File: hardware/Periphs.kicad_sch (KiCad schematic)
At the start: 0 parts

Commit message: poop
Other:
- note added: "CAN -> SPI TCAN4550-Q1 Add ESD/TVS for accidental 24V on CAN line + n shit"
- note removed: "CAN -> SPI n shit"
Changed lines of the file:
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@@
 	(generator_version "10.0")
 	(paper "A4")
-	(text "CAN -> SPI\nn shit"
+	(text "CAN -> SPI\n	TCAN4550-Q1\n	Add ESD/TVS for accidental 24V on CAN line\n\n\n+ n shit\n	"
 		(exclude_from_sim no)
-		(at 129.032 96.52 0)
+		(at 86.868 85.09 0)
 		(effects
 			(font

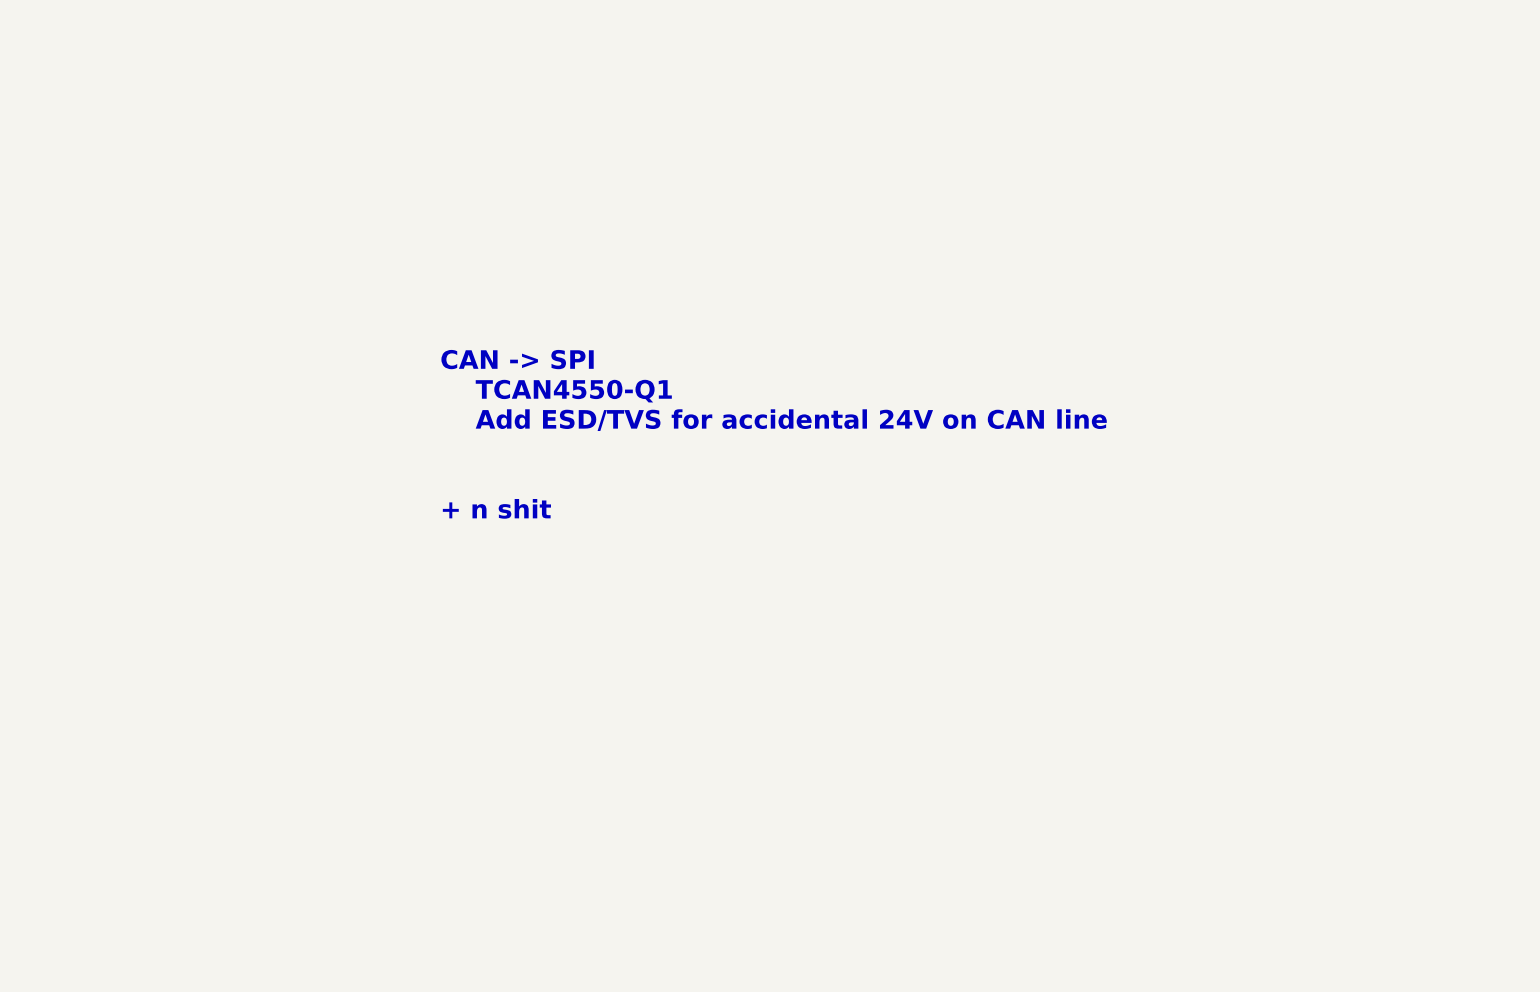
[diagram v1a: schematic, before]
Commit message: added can spi
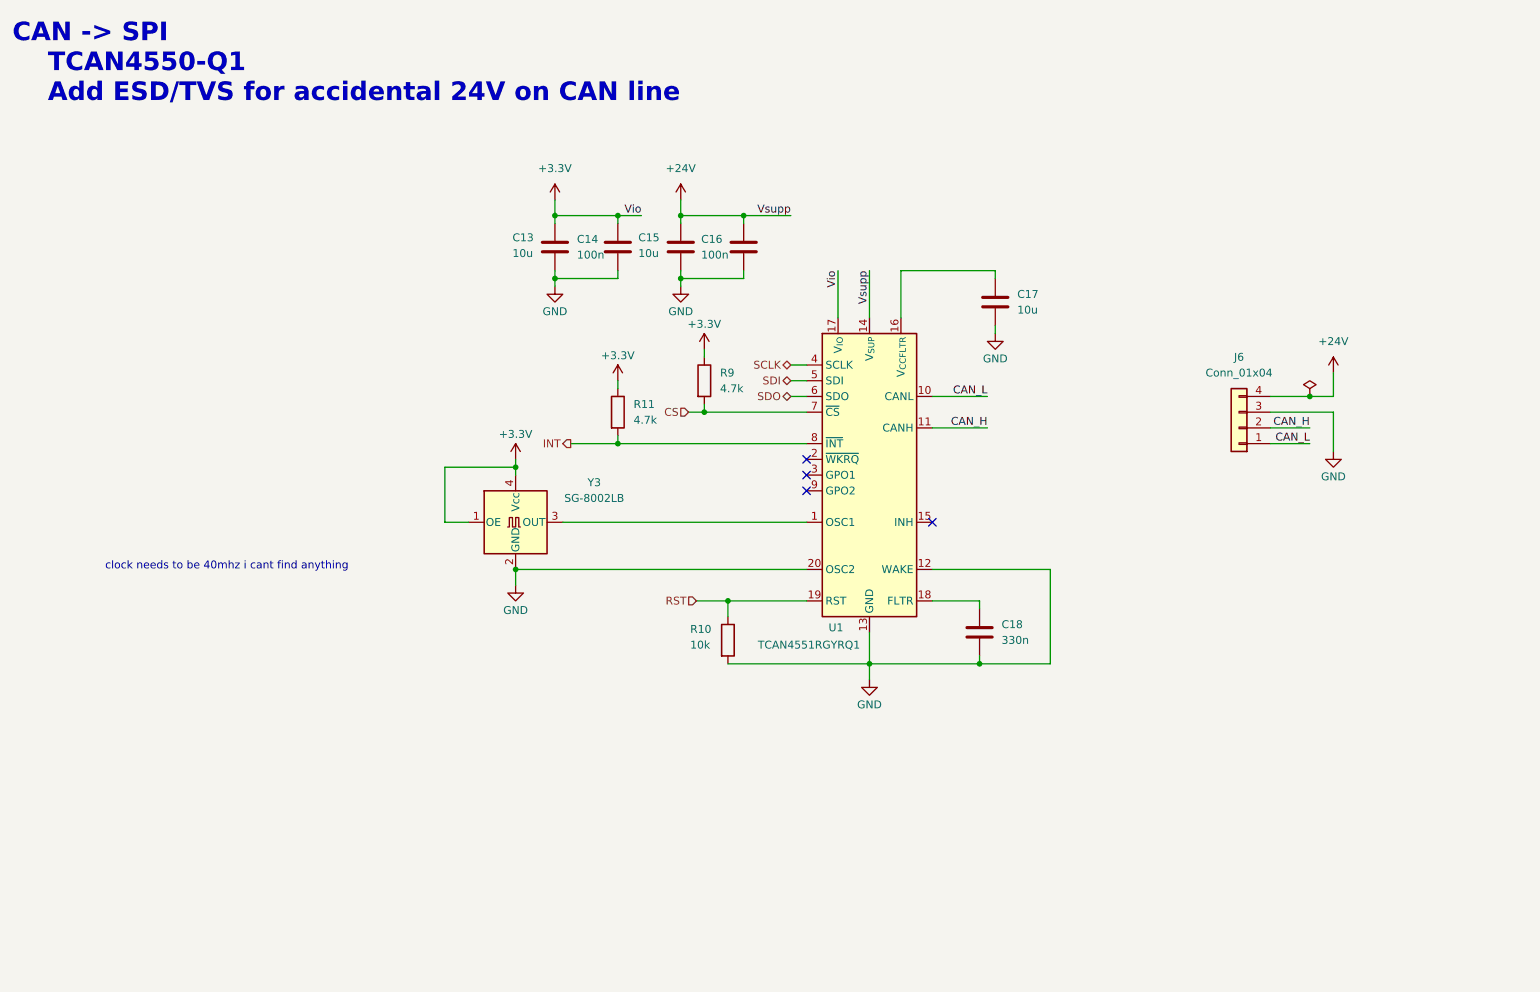
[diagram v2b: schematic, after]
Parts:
- added C13, C15, C17: 10u, symbol Device:C
- added C14, C16: 100n, symbol Device:C
- added C18: 330n, symbol Device:C
- added J6: Conn_01x04, symbol Connector_Generic:Conn_01x04
- added R10: 10k, symbol Device:R
- added R11, R9: 4.7k, symbol Device:R
- added U1: TCAN4551RGYRQ1, Package_DFN_QFN:Texas_RGY_R-PVQFN-N20_EP2.05x3.05mm, symbol Interface_CAN_LIN:TCAN4551RGYRQ1
- added Y3: SG-8002LB, Oscillator:Oscillator_SMD_SeikoEpson_SG8002LB-4Pin_5.0x3.2mm, symbol Oscillator:SG-8002LB
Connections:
- new net: U1.1 (OSC1), Y3.3 (OUT)
- new net: C18.1, U1.18 (FLTR)
- new net: C17.1, U1.16 (V_{CCFLTR})
- new net +24V: C15.1, C16.1, J6.4 (Pin_4), U1.14 (V_{SUP})
- new net +3.3V: C13.1, C14.1, R11.1, R9.1, U1.17 (V_{IO}), Y3.1 (OE), Y3.4 (Vcc)
- new net CAN_H: J6.2 (Pin_2), U1.11 (CANH)
- new net CAN_L: J6.1 (Pin_1), U1.10 (CANL)
- new net CS: R9.2, U1.7 (~{CS})
- new net GND: C13.2, C14.2, C15.2, C16.2, C17.2, C18.2, J6.3 (Pin_3), R10.2, U1.12 (WAKE), U1.13 (GND), U1.20 (OSC2), U1.21 (GND), Y3.2 (GND)
- new net INT: R11.2, U1.8 (~{INT})
- new net RST: R10.1, U1.19 (RST)
- new net SCLK: U1.4 (SCLK)
- new net SDI: U1.5 (SDI)
- new net SDO: U1.6 (SDO)
- no-connect marks 0 -> 4
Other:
- note added: "CAN -> SPI TCAN4550-Q1 Add ESD/TVS for accidental 24V on CAN line"
- note added: "clock needs to be 40mhz i cant find anything"
- note removed: "CAN -> SPI TCAN4550-Q1 Add ESD/TVS for accidental 24V on CAN line + n shit"

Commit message: some changes`
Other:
- moved on the sheet: C18, Y3
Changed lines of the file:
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@@
 	)
 	(junction
-		(at 99.06 104.14)
+		(at 115.57 83.82)
 		(diameter 0)
 		(color 0 0 0 0)
 	)
 	(junction
-		(at 115.57 83.82)
+		(at 96.52 105.41)
 		(diameter 0)
 		(color 0 0 0 0)
@@
 	)
 	(junction
-		(at 173.99 119.38)
+		(at 96.52 87.63)
 		(diameter 0)
 		(color 0 0 0 0)
 	)
 	(junction
-		(at 99.06 87.63)
+		(at 105.41 46.99)
 		(diameter 0)
 		(color 0 0 0 0)
 	)
 	(junction
-		(at 105.41 46.99)
+		(at 175.26 119.38)
 		(diameter 0)
 		(color 0 0 0 0)
@@
 	(wire
 		(pts
-			(xy 173.99 109.22) (xy 173.99 110.49)
+			(xy 175.26 109.22) (xy 175.26 110.49)
 		)
 		(stroke
@@
 	(wire
 		(pts
-			(xy 99.06 86.36) (xy 99.06 87.63)
+			(xy 96.52 86.36) (xy 96.52 87.63)
 		)
 		(stroke
@@
 	(wire
 		(pts
-			(xy 166.37 109.22) (xy 173.99 109.22)
+			(xy 139.7 105.41) (xy 139.7 104.14)
 		)
 		(stroke
@@
 	(wire
 		(pts
-			(xy 125.73 57.15) (xy 135.89 57.15)
+			(xy 166.37 109.22) (xy 175.26 109.22)
 		)
 		(stroke
@@
 	(wire
 		(pts
-			(xy 105.41 44.45) (xy 105.41 46.99)
+			(xy 125.73 57.15) (xy 135.89 57.15)
 		)
 		(stroke
@@
 	(wire
 		(pts
-			(xy 156.21 119.38) (xy 173.99 119.38)
+			(xy 105.41 44.45) (xy 105.41 46.99)
 		)
 		(stroke
@@
 	(wire
 		(pts
-			(xy 105.41 46.99) (xy 115.57 46.99)
+			(xy 156.21 119.38) (xy 175.26 119.38)
 		)
 		(stroke
@@
 	(wire
 		(pts
-			(xy 220.98 83.82) (xy 227.33 83.82)
+			(xy 105.41 46.99) (xy 115.57 46.99)
 		)
 		(stroke
@@
 	(wire
 		(pts
-			(xy 173.99 118.11) (xy 173.99 119.38)
+			(xy 220.98 83.82) (xy 227.33 83.82)
 		)
 		(stroke
@@
 	(wire
 		(pts
-			(xy 185.42 119.38) (xy 173.99 119.38)
+			(xy 125.73 48.26) (xy 125.73 46.99)
 		)
 		(stroke
@@
 	(wire
 		(pts
-			(xy 99.06 104.14) (xy 146.05 104.14)
+			(xy 105.41 57.15) (xy 105.41 58.42)
 		)
 		(stroke
@@
 	(wire
 		(pts
-			(xy 125.73 48.26) (xy 125.73 46.99)
+			(xy 125.73 57.15) (xy 125.73 58.42)
 		)
 		(stroke
@@
 	(wire
 		(pts
-			(xy 105.41 57.15) (xy 105.41 58.42)
+			(xy 156.21 119.38) (xy 156.21 121.92)
 		)
 		(stroke
@@
 	(wire
 		(pts
-			(xy 125.73 57.15) (xy 125.73 58.42)
+			(xy 96.52 105.41) (xy 139.7 105.41)
 		)
 		(stroke
@@
 	(wire
 		(pts
-			(xy 156.21 119.38) (xy 156.21 121.92)
+			(xy 143.51 73.66) (xy 146.05 73.66)
 		)
 		(stroke
@@
 	(wire
 		(pts
-			(xy 143.51 73.66) (xy 146.05 73.66)
+			(xy 129.54 77.47) (xy 129.54 78.74)
 		)
 		(stroke
@@
 	(wire
 		(pts
-			(xy 129.54 77.47) (xy 129.54 78.74)
+			(xy 127 78.74) (xy 129.54 78.74)
 		)
 		(stroke
@@
 	(wire
 		(pts
-			(xy 127 78.74) (xy 129.54 78.74)
+			(xy 125.73 44.45) (xy 125.73 46.99)
 		)
 		(stroke
@@
 	(wire
 		(pts
-			(xy 125.73 44.45) (xy 125.73 46.99)
+			(xy 125.73 46.99) (xy 135.89 46.99)
 		)
 		(stroke
@@
 	(wire
 		(pts
-			(xy 125.73 46.99) (xy 135.89 46.99)
+			(xy 85.09 87.63) (xy 96.52 87.63)
 		)
 		(stroke
@@
 	(wire
 		(pts
-			(xy 87.63 87.63) (xy 99.06 87.63)
+			(xy 156.21 55.88) (xy 156.21 63.5)
 		)
 		(stroke
@@
 	(wire
 		(pts
-			(xy 156.21 55.88) (xy 156.21 63.5)
+			(xy 175.26 118.11) (xy 175.26 119.38)
 		)
 		(stroke
@@
 	(wire
 		(pts
-			(xy 91.44 96.52) (xy 87.63 96.52)
+			(xy 88.9 96.52) (xy 85.09 96.52)
 		)
 		(stroke
@@
 	(wire
 		(pts
-			(xy 87.63 96.52) (xy 87.63 87.63)
+			(xy 85.09 96.52) (xy 85.09 87.63)
 		)
 		(stroke
@@
 	(wire
 		(pts
-			(xy 133.35 109.22) (xy 146.05 109.22)
+			(xy 139.7 104.14) (xy 146.05 104.14)
 		)
 		(stroke
@@
 	(wire
 		(pts
-			(xy 99.06 104.14) (xy 99.06 106.68)
+			(xy 96.52 105.41) (xy 96.52 104.14)
+		)
+		(stroke
+			(width 0)
+			(type default)
+		)
+	)
+	(wire
+		(pts
+			(xy 133.35 109.22) (xy 146.05 109.22)
 		)
 		(stroke
@@
 	(wire
 		(pts
-			(xy 106.68 96.52) (xy 146.05 96.52)
+			(xy 104.14 96.52) (xy 146.05 96.52)
 		)
 		(stroke
@@
 	(wire
 		(pts
+			(xy 175.26 119.38) (xy 185.42 119.38)
+		)
+		(stroke
+			(width 0)
+			(type default)
+		)
+	)
+	(wire
+		(pts
 			(xy 220.98 76.2) (xy 227.33 76.2)
 		)
@@
 	(wire
 		(pts
-			(xy 99.06 87.63) (xy 99.06 88.9)
+			(xy 96.52 105.41) (xy 96.52 107.95)
+		)
+		(stroke
+			(width 0)
+			(type default)
+		)
+	)
+	(wire
+		(pts
+			(xy 96.52 87.63) (xy 96.52 88.9)
 		)
 		(stroke
@@
 	)
 	(image
-		(at 157.48 129.54)
+		(at 157.48 132.08)
 		(scale 0.238773)
 		(data "iVBORw0KGgoAAAANSUhEUgAABqIAAACCCAYAAAAt69luAAAMTWlDQ1BJQ0MgUHJvZmlsZQAASImV"
@@
 		)
 		(property "Value" "GND"
-			(at 156.21 125.984 0)
+			(at 156.21 125.476 0)
 			(show_name no)
 			(do_not_autoplace no)
@@
 	(symbol
 		(lib_id "power:+3.3V")
-		(at 99.06 86.36 0)
+		(at 96.52 86.36 0)
 		(unit 1)
 		(body_style 1)
@@
 		(dnp no)
 		(property "Reference" "#PWR039"
-			(at 99.06 90.17 0)
+			(at 96.52 90.17 0)
 			(hide yes)
 			(show_name no)
@@
 		)
 		(property "Value" "+3.3V"
-			(at 99.06 82.296 0)
+			(at 96.52 82.804 0)
 			(show_name no)
 			(do_not_autoplace no)
@@
 		)
 		(property "Footprint" ""
-			(at 99.06 86.36 0)
+			(at 96.52 86.36 0)
 			(hide yes)
 			(show_name no)
@@
 		)
 		(property "Datasheet" ""
-			(at 99.06 86.36 0)
+			(at 96.52 86.36 0)
 			(hide yes)
 			(show_name no)
@@
 		)
 		(property "Description" "Power symbol creates a global label with name \"+3.3V\""
-			(at 99.06 86.36 0)
+			(at 96.52 86.36 0)
 			(hide yes)
 			(show_name no)
@@
 	(symbol
 		(lib_id "Oscillator:SG-8002LB")
-		(at 99.06 96.52 0)
+		(at 96.52 96.52 0)
 		(unit 1)
 		(body_style 1)
@@
 		(in_pos_files yes)
 		(dnp no)
-		(fields_autoplaced yes)
 		(property "Reference" "Y3"
-			(at 111.76 90.0998 0)
+			(at 107.696 97.79 0)
 			(show_name no)
 			(do_not_autoplace no)
@@
 		)
 		(property "Value" "SG-8002LB"
-			(at 111.76 92.6398 0)
+			(at 107.696 100.33 0)
 			(show_name no)
 			(do_not_autoplace no)
@@
 		)
 		(property "Footprint" "Oscillator:Oscillator_SMD_SeikoEpson_SG8002LB-4Pin_5.0x3.2mm"
-			(at 116.84 105.41 0)
+			(at 114.3 105.41 0)
 			(hide yes)
 			(show_name no)
@@
 		)
 		(property "Datasheet" "https://support.epson.biz/td/api/doc_check.php?dl=brief_SG-8002LB&lang=en"
-			(at 96.52 96.52 0)
+			(at 93.98 96.52 0)
 			(hide yes)
 			(show_name no)
@@
 		)
 		(property "Description" "CMOS Clock Oscillator 1 to 125 MHz"
-			(at 99.06 96.52 0)
+			(at 96.52 96.52 0)
 			(hide yes)
 			(show_name no)
@@
 	(symbol
 		(lib_id "Device:C")
-		(at 173.99 114.3 0)
+		(at 175.26 114.3 0)
 		(unit 1)
 		(body_style 1)
@@
 		(dnp no)
 		(property "Reference" "C18"
-			(at 177.546 113.03 0)
+			(at 177.8 113.03 0)
 			(show_name no)
 			(do_not_autoplace no)
@@
 		)
 		(property "Value" "330n"
-			(at 177.546 115.57 0)
+			(at 177.8 115.57 0)
 			(show_name no)
 			(do_not_autoplace no)
@@
 		)
 		(property "Footprint" ""
-			(at 174.9552 118.11 0)
+			(at 176.2252 118.11 0)
 			(hide yes)
 			(show_name no)
@@
 		)
 		(property "Datasheet" ""
-			(at 173.99 114.3 0)
+			(at 175.26 114.3 0)
 			(hide yes)
 			(show_name no)
@@
 		)
 		(property "Description" "Unpolarized capacitor"
-			(at 173.99 114.3 0)
+			(at 175.26 114.3 0)
 			(hide yes)
 			(show_name no)
@@
 	(symbol
 		(lib_id "power:GND")
-		(at 99.06 106.68 0)
+		(at 96.52 107.95 0)
 		(unit 1)
 		(body_style 1)
@@
 		(dnp no)
 		(property "Reference" "#PWR040"
-			(at 99.06 113.03 0)
+			(at 96.52 114.3 0)
 			(hide yes)
 			(show_name no)
@@
 		)
 		(property "Value" "GND"
-			(at 99.06 110.744 0)
+			(at 96.52 112.014 0)
 			(show_name no)
 			(do_not_autoplace no)
@@
 		)
 		(property "Footprint" ""
-			(at 99.06 106.68 0)
+			(at 96.52 107.95 0)
 			(hide yes)
 			(show_name no)
@@
 		)
 		(property "Datasheet" ""
-			(at 99.06 106.68 0)
+			(at 96.52 107.95 0)
 			(hide yes)
 			(show_name no)
@@
 		)
 		(property "Description" "Power symbol creates a global label with name \"GND\" , ground"
-			(at 99.06 106.68 0)
+			(at 96.52 107.95 0)
 			(hide yes)
 			(show_name no)

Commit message: clock added
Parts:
- removed Y3: SG-8002LB, Oscillator:Oscillator_SMD_SeikoEpson_SG8002LB-4Pin_5.0x3.2mm, symbol Oscillator:SG-8002LB
- added C20, C21: 18p, symbol Device:C
- added Y2: 7M40000005, 7M27120MAAJT, symbol 7M40000005:7M40000005
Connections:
- net +24V: no longer J6.4 (Pin_4)
- net GND: now also C20.2, C21.2, Y2.2 (GND_1), Y2.4 (GND_2); no longer U1.20 (OSC2)
- net at U1.1 (OSC1): now also C20.1, Y2.3 (CRYSTAL)
- new net: C21.1, U1.20 (OSC2), Y2.1 (CRYSTLA)
- new net +12V: J6.4 (Pin_4)
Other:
- note added: "add power protection block"

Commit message: fix
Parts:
- added JP1: Jumper_2_Small_Open, symbol Jumper:Jumper_2_Small_Open
- added R3: 120, symbol Device:R
- C20, C21: value 18p -> 12p
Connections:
- net CAN_H: now also JP1.1 (A)
- net CAN_L: now also R3.2
- net +24V renamed +12v
- new net: JP1.2 (B), R3.1
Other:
- moved on the sheet: C20

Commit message: mika review usb
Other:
- added sheet USBPD (PD.kicad_sch)
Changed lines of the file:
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@@
 		(in_pos_files yes)
 		(dnp no)
-		(fields_autoplaced yes)
 		(property "Reference" "#PWR033"
 			(at 105.41 48.26 0)
@@
 		)
 		(property "Value" "+3.3V"
-			(at 105.41 39.37 0)
+			(at 105.41 40.132 0)
 			(show_name no)
 			(do_not_autoplace no)
@@
 		(in_pos_files yes)
 		(dnp no)
-		(fields_autoplaced yes)
 		(property "Reference" "#PWR034"
 			(at 125.73 48.26 0)
@@
 		)
 		(property "Value" "+12v"
-			(at 128.27 43.1799 0)
+			(at 123.698 40.894 0)
 			(show_name no)
 			(do_not_autoplace no)
@@
 				)
 			)
+		)
+	)
+	(sheet
+		(at 38.1 137.16)
+		(size 60.96 30.48)
+		(exclude_from_sim no)
+		(in_bom yes)
+		(on_board yes)
+		(dnp no)
+		(fields_autoplaced yes)
+		(stroke
+			(width 0.1524)
+			(type solid)
+		)
+		(fill
+			(color 0 0 0 0)
+		)
+		(property "Sheetname" "USBPD"
+			(at 38.1 136.4484 0)
+			(show_name no)
+			(do_not_autoplace no)
+			(effects
+				(font
+					(size 1.27 1.27)
+				)
+				(justify left bottom)
+			)
+		)
+		(property "Sheetfile" "PD.kicad_sch"
+			(at 38.1 168.2246 0)
+			(show_name no)
+			(do_not_autoplace no)
+			(effects
+				(font
+					(size 1.27 1.27)
+				)
+				(justify left top)
+			)
+		)
+		(instances
+			(project "OTTER"
+				(path "/db2a353b-4a3a-4ce7-8df7-bc33bc3b7cc7/eb093129-c761-474d-99d3-e85b871e9c74"
+					(page "10")
+				)
+			)

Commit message: matthew review or get touched
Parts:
- removed R11: 4.7k, symbol Device:R
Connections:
- net +12v renamed +20v
- net INT: no longer names the net of U1.8 (~{INT})
- no-connect marks 4 -> 5
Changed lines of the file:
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@@
 	)
 	(junction
-		(at 115.57 83.82)
-		(diameter 0)
-		(color 0 0 0 0)
-	)
-	(junction
 		(at 255.27 76.2)
 		(diameter 0)
@@
 	)
 	(no_connect
+		(at 146.05 83.82)
+	)
+	(no_connect
 		(at 146.05 91.44)
 	)
@@
 	(wire
 		(pts
-			(xy 115.57 73.66) (xy 115.57 74.93)
-		)
-		(stroke
-			(width 0)
-			(type default)
-		)
-	)
-	(wire
-		(pts
-			(xy 115.57 83.82) (xy 146.05 83.82)
-		)
-		(stroke
-			(width 0)
-			(type default)
-		)
-	)
-	(wire
-		(pts
 			(xy 161.29 55.88) (xy 176.53 55.88)
 		)
@@
 	(wire
 		(pts
-			(xy 107.95 83.82) (xy 115.57 83.82)
-		)
-		(stroke
-			(width 0)
-			(type default)
-		)
-	)
-	(wire
-		(pts
 			(xy 220.98 78.74) (xy 231.14 78.74)
 		)
@@
 	(wire
 		(pts
-			(xy 115.57 82.55) (xy 115.57 83.82)
-		)
-		(stroke
-			(width 0)
-			(type default)
-		)
-	)
-	(wire
-		(pts
 			(xy 176.53 55.88) (xy 176.53 57.15)
 		)
@@
 		)
 	)
-	(hierarchical_label "INT"
-		(shape output)
-		(at 107.95 83.82 180)
-		(effects
-			(font
-				(size 1.27 1.27)
-			)
-			(justify right)
-		)
-	)
 	(hierarchical_label "SCLK"
 		(shape bidirectional)
@@
 	)
 	(symbol
-		(lib_id "Device:R")
-		(at 115.57 78.74 0)
-		(unit 1)
-		(body_style 1)
-		(exclude_from_sim no)
-		(in_bom yes)
-		(on_board yes)
-		(in_pos_files yes)
-		(dnp no)
-		(fields_autoplaced yes)
-		(property "Reference" "R11"
-			(at 118.11 77.4699 0)
-			(show_name no)
-			(do_not_autoplace no)
-			(effects
-				(font
-					(size 1.27 1.27)
-				)
-				(justify left)
-			)
-		)
-		(property "Value" "4.7k"
-			(at 118.11 80.0099 0)
-			(show_name no)
-			(do_not_autoplace no)
-			(effects
-				(font
-					(size 1.27 1.27)
-				)
-				(justify left)
-			)
-		)
-		(property "Footprint" ""
-			(at 113.792 78.74 90)
-			(hide yes)
-			(show_name no)
-			(do_not_autoplace no)
-			(effects
-				(font
-					(size 1.27 1.27)
-				)
-			)
-		)
-		(property "Datasheet" ""
-			(at 115.57 78.74 0)
-			(hide yes)
-			(show_name no)
-			(do_not_autoplace no)
-			(effects
-				(font
-					(size 1.27 1.27)
-				)
-			)
-		)
-		(property "Description" "Resistor"
-			(at 115.57 78.74 0)
-			(hide yes)
-			(show_name no)
-			(do_not_autoplace no)
-			(effects
-				(font
-					(size 1.27 1.27)
-				)
-			)
-		)
-		(pin "2"
-		)
-		(pin "1"
-		)
-		(instances
-			(project "OTTER"
-				(path "/db2a353b-4a3a-4ce7-8df7-bc33bc3b7cc7/eb093129-c761-474d-99d3-e85b871e9c74"
-					(reference "R11")
-					(unit 1)
-				)
-			)
-		)
-	)
-	(symbol
 		(lib_id "power:PWR_FLAG")
 		(at 255.27 76.2 0)
@@
 			)
 		)
-		(property "Value" "+12v"
+		(property "Value" "+20v"
 			(at 123.698 40.894 0)
 			(show_name no)
@@
 					(unit 1)
 				)
-			)
-		)
-	)
-	(symbol
-		(lib_id "power:+3.3V")
-		(at 115.57 73.66 0)
-		(unit 1)
-		(body_style 1)
-		(exclude_from_sim no)
-		(in_bom yes)
-		(on_board yes)
-		(in_pos_files yes)
-		(dnp no)
-		(property "Reference" "#PWR037"
-			(at 115.57 77.47 0)
-			(hide yes)
-			(show_name no)
-			(do_not_autoplace no)
-			(effects
-				(font
-					(size 1.27 1.27)
-				)
-			)
-		)
-		(property "Value" "+3.3V"
-			(at 115.57 69.596 0)
-			(show_name no)
-			(do_not_autoplace no)
-			(effects
-				(font
-					(size 1.27 1.27)
-				)
-			)
-		)
-		(property "Footprint" ""
-			(at 115.57 73.66 0)
-			(hide yes)
-			(show_name no)
-			(do_not_autoplace no)
-			(effects
-				(font
-					(size 1.27 1.27)
-				)
-			)
-		)
-		(property "Datasheet" ""
-			(at 115.57 73.66 0)
-			(hide yes)
-			(show_name no)
-			(do_not_autoplace no)
-			(effects
-				(font
-					(size 1.27 1.27)
-				)
-			)
-		)
-		(property "Description" "Power symbol creates a global label with name \"+3.3V\""
-			(at 115.57 73.66 0)
-			(hide yes)
-			(show_name no)
-			(do_not_autoplace no)
-			(effects
-				(font
-					(size 1.27 1.27)
-				)
-			)
-		)
-		(pin "1"
-		)
-		(instances
-			(project "OTTER"
-				(path "/db2a353b-4a3a-4ce7-8df7-bc33bc3b7cc7/eb093129-c761-474d-99d3-e85b871e9c74"
-					(reference "#PWR037")
-					(unit 1)
-				)

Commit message: starting layout
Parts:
- C13, C14, C15, C16, C17, C18, C20, C21: footprint (none) -> Capacitor_SMD:C_0603_1608Metric_Pad1.08x0.95mm_HandSolder
- J6: footprint (none) -> Connector_PinSocket_2.54mm:PinSocket_1x04_P2.54mm_Vertical
- JP1: footprint (none) -> Connector_PinHeader_2.54mm:PinHeader_1x02_P2.54mm_Vertical
- R10, R3: footprint (none) -> Resistor_SMD:R_0603_1608Metric_Pad0.98x0.95mm_HandSolder
- R9: value 4.7k -> 10k; footprint (none) -> Resistor_SMD:R_0603_1608Metric_Pad0.98x0.95mm_HandSolder
- Y2: footprint 7M27120MAAJT -> 7M40000005:7M27120MAAJT
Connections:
- net +20v renamed +20V
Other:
- sheet USBPD ports: added +20v, GND; removed none
- moved on the sheet: C13, C14
